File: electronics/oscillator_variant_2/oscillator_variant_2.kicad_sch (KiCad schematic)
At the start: 51 parts, among them J1 module_2x15_left_input, J2 module_2x15_right_input, J3 Coax, Q1 BC817, U1 TL081, U2 LME49720, U3 TL082, U4 TL431

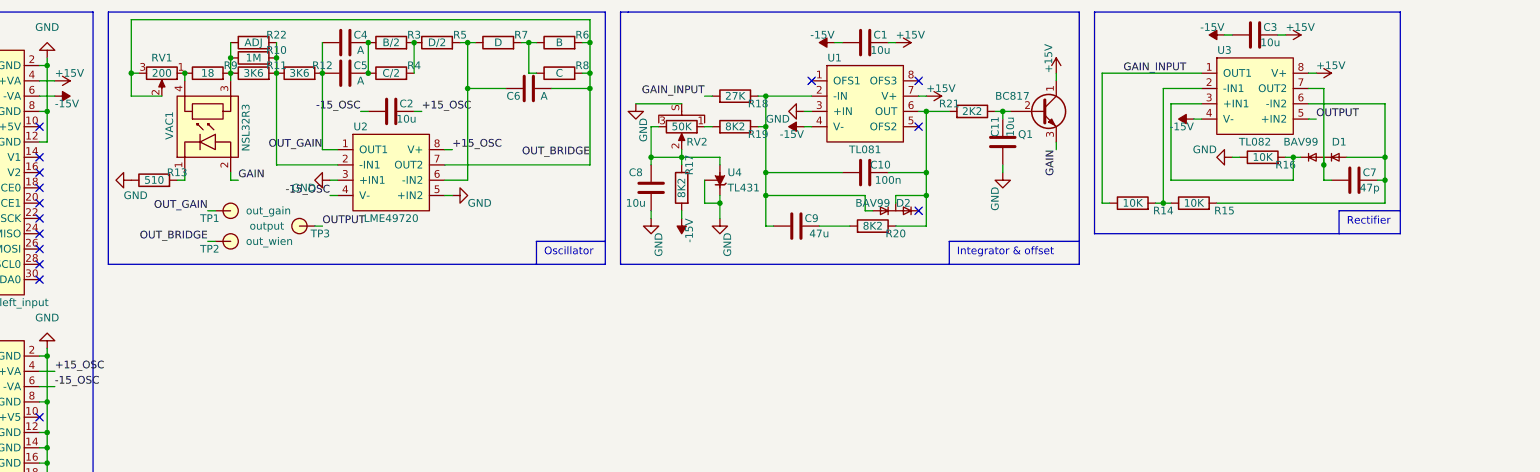
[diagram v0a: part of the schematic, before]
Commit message: added oscillator variant with dual single opamp
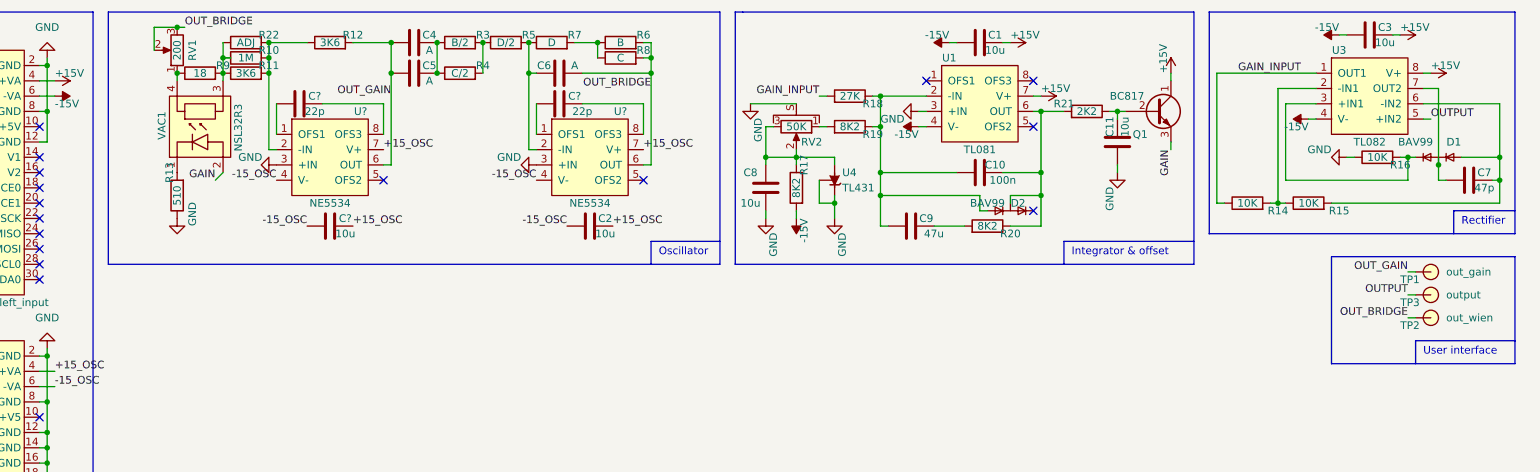
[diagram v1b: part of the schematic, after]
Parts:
- removed U2: LME49720, Package_DIP:DIP-8_W7.62mm_Socket, symbol SquantorGenericAnalog:opamp_dual_8pin
- added C? (x2): 22p, SquantorRcl:C_0805+0603, symbol Device:C
- added C?: 10u, SquantorRcl:C_0805+0603, symbol Device:C
- added U? (x2): NE5534, Package_DIP:DIP-8_W7.62mm_Socket, symbol SquantorGenericAnalog:opamp_single_8pin
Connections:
- net +15_OSC: now also C?.2, U?.7 (V+), U?.7 (V+)
- net -15_OSC: now also C?.1, U?.4 (V-), U?.4 (V-)
- net GND: now also U?.3 (+IN), U?.3 (+IN)
- net OUT_BRIDGE: now also U?.6 (OUT)
- net OUT_GAIN: now also U?.6 (OUT)
- net at R10.2, R11.2, R12.1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: now also U?.2 (-IN)
- net at C6.1, R5.2, R7.1: now also U?.2 (-IN)
- new net: C?.1, U?.1 (OFS1) (x2)
- new net: C?.2, U?.8 (OFS3) (x2)
- no-connect marks 26 -> 28
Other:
- note added: "User interface"
- moved on the sheet: C1, C10, C11, C2, C3, C4, C5, C6, C7, C8, C9, D1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

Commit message: silk placement completed
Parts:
- added N3: Freq, SquantorLabels:Label_Note_medium, symbol SquantorLabels:Label
- gave numbers to parts that had none: 5
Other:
- moved on the sheet: N1, N2
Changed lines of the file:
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@@
+    (stroke (width 0) (type default) (color 0 0 0 0))
+  )
+  (polyline (pts (xy 31.75 191.77) (xy 31.75 195.58))
     (stroke (width 0) (type default) (color 0 0 0 0))
   )
@@
     (stroke (width 0) (type default) (color 0 0 0 0))
   )
-  (polyline (pts (xy 35.56 177.8) (xy 15.24 177.8))
+  (polyline (pts (xy 52.07 177.8) (xy 15.24 177.8))
     (stroke (width 0) (type default) (color 0 0 0 0))
   )
@@
     (stroke (width 0) (type default) (color 0 0 0 0))
   )
-  (polyline (pts (xy 35.56 195.58) (xy 35.56 177.8))
+  (polyline (pts (xy 52.07 195.58) (xy 52.07 177.8))
     (stroke (width 0) (type default) (color 0 0 0 0))
   )
@@
     (stroke (width 0) (type default) (color 0 0 0 0))
   )
-  (polyline (pts (xy 15.24 195.58) (xy 35.56 195.58))
+  (polyline (pts (xy 15.24 195.58) (xy 52.07 195.58))
     (stroke (width 0) (type default) (color 0 0 0 0))
   )
@@
     (stroke (width 0) (type default) (color 0 0 0 0))
   )
-  (polyline (pts (xy 15.24 191.77) (xy 35.56 191.77))
+  (polyline (pts (xy 31.75 191.77) (xy 52.07 191.77))
     (stroke (width 0) (type default) (color 0 0 0 0))
   )
@@
     (effects (font (size 1.27 1.27)) (justify left bottom))
   )
-  (text "Logos and version" (at 16.51 194.31 0)
+  (text "Logos and version" (at 33.02 194.31 0)
     (effects (font (size 1.27 1.27)) (justify left bottom))
   )
@@
     (effects (font (size 1.27 1.27)) (justify right bottom))
   )
-  (symbol (lib_id "SquantorLabels:VYYYYMMDD") (at 26.67 189.23 0) (unit 1)
-    (in_bom yes) (on_board yes)
-    (property "Reference" "N1" (id 0) (at 25.4 186.69 0)
+  (symbol (lib_id "SquantorLabels:VYYYYMMDD") (at 43.18 189.23 0) (unit 1)
+    (in_bom yes) (on_board yes)
+    (property "Reference" "N1" (id 0) (at 41.91 186.69 0)
       (effects (font (size 1.524 1.524)) (justify left))
     )
-    (property "Value" "20220501" (id 1) (at 20.32 189.23 0)
+    (property "Value" "20220501" (id 1) (at 36.83 189.23 0)
       (effects (font (size 1.524 1.524)) (justify left))
     )
-    (property "Footprint" "SquantorLabels:Label_Generic" (id 2) (at 26.67 189.23 0)
+    (property "Footprint" "SquantorLabels:Label_Generic" (id 2) (at 43.18 189.23 0)
       (effects (font (size 1.524 1.524)) hide)
     )
-    (property "Datasheet" "" (id 3) (at 26.67 189.23 0)
+    (property "Datasheet" "" (id 3) (at 43.18 189.23 0)
       (effects (font (size 1.524 1.524)) hide)
     )
   )
-  (symbol (lib_id "SquantorLabels:OHWLOGO") (at 20.32 181.61 0) (unit 1)
-    (in_bom yes) (on_board yes)
-    (property "Reference" "N2" (id 0) (at 23.5712 180.2638 0)
+  (symbol (lib_id "SquantorLabels:OHWLOGO") (at 36.83 181.61 0) (unit 1)
+    (in_bom yes) (on_board yes)
+    (property "Reference" "N2" (id 0) (at 40.0812 180.2638 0)
       (effects (font (size 1.524 1.524)) (justify left))
     )
-    (property "Value" "OHWLOGO" (id 1) (at 23.5712 182.9562 0)
+    (property "Value" "OHWLOGO" (id 1) (at 40.0812 182.9562 0)
       (effects (font (size 1.524 1.524)) (justify left))
     )
-    (property "Footprint" "Symbol:OSHW-Symbol_6.7x6mm_SilkScreen" (id 2) (at 20.32 181.61 0)
+    (property "Footprint" "Symbol:OSHW-Symbol_6.7x6mm_SilkScreen" (id 2) (at 36.83 181.61 0)
       (effects (font (size 1.524 1.524)) hide)
     )
-    (property "Datasheet" "" (id 3) (at 20.32 181.61 0)
+    (property "Datasheet" "" (id 3) (at 36.83 181.61 0)
       (effects (font (size 1.524 1.524)) hide)
     )
@@
   (symbol (lib_id "Device:C") (at 81.28 29.21 90) (unit 1)
     (in_bom yes) (on_board yes)
-    (property "Reference" "C?" (id 0) (at 83.82 27.94 90))
+    (property "Reference" "C12" (id 0) (at 83.82 27.94 90))
     (property "Value" "22p" (id 1) (at 83.82 30.48 90))
     (property "Footprint" "SquantorRcl:C_0805+0603" (id 2) (at 85.09 28.2448 0)
@@
   (symbol (lib_id "power:GND") (at 77.47 39.37 270) (unit 1)
     (in_bom yes) (on_board yes)
-    (property "Reference" "#PWR?" (id 0) (at 71.12 39.37 0)
+    (property "Reference" "#PWR0107" (id 0) (at 71.12 39.37 0)
       (effects (font (size 1.27 1.27)) hide)
     )
@@
   (symbol (lib_id "power:GND") (at 120.65 39.37 270) (unit 1)
     (in_bom yes) (on_board yes)
-    (property "Reference" "#PWR?" (id 0) (at 114.3 39.37 0)
+    (property "Reference" "#PWR0105" (id 0) (at 114.3 39.37 0)
       (effects (font (size 1.27 1.27)) hide)
     )
@@
   (symbol (lib_id "Device:C") (at 86.36 49.53 90) (unit 1)
     (in_bom yes) (on_board yes)
-    (property "Reference" "C?" (id 0) (at 88.9 48.26 90))
+    (property "Reference" "C13" (id 0) (at 88.9 48.26 90))
     (property "Value" "10u" (id 1) (at 88.9 50.8 90))
     (property "Footprint" "SquantorRcl:C_0805+0603" (id 2) (at 90.17 48.5648 0)
@@
   (symbol (lib_id "SquantorGenericAnalog:opamp_single_8pin") (at 129.54 38.1 0) (unit 1)
     (in_bom yes) (on_board yes)
-    (property "Reference" "U?" (id 0) (at 134.62 30.48 0))
+    (property "Reference" "U5" (id 0) (at 134.62 30.48 0))
     (property "Value" "NE5534" (id 1) (at 129.54 45.72 0))
     (property "Footprint" "Package_DIP:DIP-8_W7.62mm_Socket" (id 2) (at 130.81 38.1 0)
@@
     )
     (pin "1")
+  )
+  (symbol (lib_id "SquantorLabels:Label") (at 24.13 181.61 0) (unit 1)
+    (in_bom yes) (on_board yes)
+    (property "Reference" "N3" (id 0) (at 22.86 180.34 0)
+      (effects (font (size 1.524 1.524)) (justify left))
+    )
+    (property "Value" "Freq" (id 1) (at 21.59 182.88 0)
+      (effects (font (size 1.524 1.524)) (justify left))
+    )
+    (property "Footprint" "SquantorLabels:Label_Note_medium" (id 2) (at 24.13 181.61 0)
+      (effects (font (size 1.524 1.524)) hide)
+    )
+    (property "Datasheet" "" (id 3) (at 24.13 181.61 0)
+      (effects (font (size 1.524 1.524)) hide)
+    )
   )
   (symbol (lib_id "Reference_Voltage:TL431LP") (at 170.18 41.91 90) (mirror x) (unit 1)
@@
   (symbol (lib_id "SquantorGenericAnalog:opamp_single_8pin") (at 86.36 38.1 0) (unit 1)
     (in_bom yes) (on_board yes)
-    (property "Reference" "U?" (id 0) (at 91.44 30.48 0))
+    (property "Reference" "U2" (id 0) (at 91.44 30.48 0))
     (property "Value" "NE5534" (id 1) (at 86.36 45.72 0))
     (property "Footprint" "Package_DIP:DIP-8_W7.62mm_Socket" (id 2) (at 87.63 38.1 0)
@@
   (symbol (lib_id "Device:C") (at 124.46 29.21 90) (unit 1)
     (in_bom yes) (on_board yes)
-    (property "Reference" "C?" (id 0) (at 127 27.94 90))
+    (property "Reference" "C14" (id 0) (at 127 27.94 90))
     (property "Value" "22p" (id 1) (at 128.27 30.48 90))
     (property "Footprint" "SquantorRcl:C_0805+0603" (id 2) (at 128.27 28.2448 0)
@@
       (reference "#PWR0104") (unit 1) (value "GND") (footprint "")
     )
+    (path "/5c88502a-1002-4c17-854f-b2d7102f5067"
+      (reference "#PWR0105") (unit 1) (value "GND") (footprint "")
+    )
     (path "/77795390-9155-4896-86aa-0181873c86a5"
       (reference "#PWR0106") (unit 1) (value "GND") (footprint "")
     )
+    (path "/1af75269-3d61-4bbc-ac5c-4f35abf226fe"
+      (reference "#PWR0107") (unit 1) (value "GND") (footprint "")
+    )
     (path "/dc6ec896-5c41-4cf2-9f5b-8e01e6b8b937"
       (reference "#PWR0108") (unit 1) (value "GND") (footprint "")
@@
       (reference "#PWR0113") (unit 1) (value "GND") (footprint "")
     )
-    (path "/1af75269-3d61-4bbc-ac5c-4f35abf226fe"
-      (reference "#PWR?") (unit 1) (value "GND") (footprint "")
-    )
-    (path "/5c88502a-1002-4c17-854f-b2d7102f5067"
-      (reference "#PWR?") (unit 1) (value "GND") (footprint "")
-    )
     (path "/9becc288-ce01-4768-9828-7cceb055ae24"
       (reference "C1") (unit 1) (value "10u") (footprint "SquantorRcl:C_0805+0603")
@@
     )
     (path "/02b2ff54-2418-4bc0-b1fb-876d0e53a8a7"
-      (reference "C?") (unit 1) (value "22p") (footprint "SquantorRcl:C_0805+0603")
+      (reference "C12") (unit 1) (value "22p") (footprint "SquantorRcl:C_0805+0603")
     )
     (path "/a8a995b7-a05a-410f-b10e-b11879a843bf"
-      (reference "C?") (unit 1) (value "10u") (footprint "SquantorRcl:C_0805+0603")
+      (reference "C13") (unit 1) (value "10u") (footprint "SquantorRcl:C_0805+0603")
     )
     (path "/f59a11c2-fb8b-4a86-abff-6583e1fcd113"
-      (reference "C?") (unit 1) (value "22p") (footprint "SquantorRcl:C_0805+0603")
+      (reference "C14") (unit 1) (value "22p") (footprint "SquantorRcl:C_0805+0603")
     )
     (path "/d02b46fd-3514-491d-82c6-c3ac88a230c3"
@@
       (reference "N2") (unit 1) (value "OHWLOGO") (footprint "Symbol:OSHW-Symbol_6.7x6mm_SilkScreen")
     )
+    (path "/bad38633-784e-4bd7-8d92-3fa5be59c443"
+      (reference "N3") (unit 1) (value "Freq") (footprint "SquantorLabels:Label_Note_medium")
+    )
     (path "/8d94cc0c-201d-408b-9763-fb9c677e462a"
       (reference "Q1") (unit 1) (value "BC817") (footprint "SquantorIC:SOT23-3")
@@
       (reference "U1") (unit 1) (value "TL081") (footprint "Package_DIP:DIP-8_W7.62mm_Socket")
     )
+    (path "/f3a55c31-28cf-4662-87ac-009b26a00e60"
+      (reference "U2") (unit 1) (value "NE5534") (footprint "Package_DIP:DIP-8_W7.62mm_Socket")
+    )
     (path "/af45fa3d-9c0d-4ca0-9093-843c207dfa9b"
       (reference "U3") (unit 1) (value "TL082") (footprint "Package_DIP:DIP-8_W7.62mm_Socket")
@@
     )
     (path "/abf3084a-1a45-4f85-82f3-6e9d78bb0883"
-      (reference "U?") (unit 1) (value "NE5534") (footprint "Package_DIP:DIP-8_W7.62mm_Socket")
-    )
-    (path "/f3a55c31-28cf-4662-87ac-009b26a00e60"
-      (reference "U?") (unit 1) (value "NE5534") (footprint "Package_DIP:DIP-8_W7.62mm_Socket")
+      (reference "U5") (unit 1) (value "NE5534") (footprint "Package_DIP:DIP-8_W7.62mm_Socket")
     )
     (path "/e72b4efd-dfaa-4a83-a78f-5c6fa864d78a"

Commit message: review completed
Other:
- note added: "output config"
- note removed: "User interface"
- moved on the sheet: J3, R1, R2, TP1, TP2, TP3

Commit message: fixed aisler warnings/errors
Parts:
- C4, C5, C6: footprint SquantorRcl:C-025_050-050X100-0805-3516-film -> SquantorRcl:C-050-050X100-0805-3516-film
- N1: value 20220501 -> 20220530
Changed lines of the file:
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@@
       (effects (font (size 1.524 1.524)) (justify left))
     )
-    (property "Value" "20220501" (id 1) (at 36.83 189.23 0)
+    (property "Value" "20220530" (id 1) (at 36.83 189.23 0)
       (effects (font (size 1.524 1.524)) (justify left))
     )
@@
     (property "Reference" "C6" (id 0) (at 121.92 22.86 90))
     (property "Value" "A" (id 1) (at 127 22.86 90))
-    (property "Footprint" "SquantorRcl:C-025_050-050X100-0805-3516-film" (id 2) (at 128.27 23.1648 0)
+    (property "Footprint" "SquantorRcl:C-050-050X100-0805-3516-film" (id 2) (at 128.27 23.1648 0)
       (effects (font (size 1.27 1.27)) hide)
     )
@@
     (property "Reference" "C5" (id 0) (at 102.87 22.86 90))
     (property "Value" "A" (id 1) (at 102.87 25.4 90))
-    (property "Footprint" "SquantorRcl:C-025_050-050X100-0805-3516-film" (id 2) (at 104.14 23.1648 0)
+    (property "Footprint" "SquantorRcl:C-050-050X100-0805-3516-film" (id 2) (at 104.14 23.1648 0)
       (effects (font (size 1.27 1.27)) hide)
     )
@@
     (property "Reference" "C4" (id 0) (at 102.87 17.78 90))
     (property "Value" "A" (id 1) (at 102.87 20.32 90))
-    (property "Footprint" "SquantorRcl:C-025_050-050X100-0805-3516-film" (id 2) (at 104.14 18.0848 0)
+    (property "Footprint" "SquantorRcl:C-050-050X100-0805-3516-film" (id 2) (at 104.14 18.0848 0)
       (effects (font (size 1.27 1.27)) hide)
     )
@@
     )
     (path "/b51ccab4-4241-4333-b251-d201fcd5e558"
-      (reference "C4") (unit 1) (value "A") (footprint "SquantorRcl:C-025_050-050X100-0805-3516-film")
+      (reference "C4") (unit 1) (value "A") (footprint "SquantorRcl:C-050-050X100-0805-3516-film")
     )
     (path "/2f8578f6-29b3-46c0-be78-3b257f29f7dd"
-      (reference "C5") (unit 1) (value "A") (footprint "SquantorRcl:C-025_050-050X100-0805-3516-film")
+      (reference "C5") (unit 1) (value "A") (footprint "SquantorRcl:C-050-050X100-0805-3516-film")
     )
     (path "/1a6a52f9-6b08-4411-9f3c-a37445b04753"
-      (reference "C6") (unit 1) (value "A") (footprint "SquantorRcl:C-025_050-050X100-0805-3516-film")
+      (reference "C6") (unit 1) (value "A") (footprint "SquantorRcl:C-050-050X100-0805-3516-film")
     )
     (path "/b63a5da9-8066-4614-a4b4-b99c80f29aec"
@@
     )
     (path "/00000000-0000-0000-0000-00005ee12bf3"
-      (reference "N1") (unit 1) (value "20220501") (footprint "SquantorLabels:Label_Generic")
+      (reference "N1") (unit 1) (value "20220530") (footprint "SquantorLabels:Label_Generic")
     )
     (path "/00000000-0000-0000-0000-00005ee13678"
